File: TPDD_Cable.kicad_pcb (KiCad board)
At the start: 2 copper layers, 10.4 x 13.2 mm, 5 parts, among them J1 Wire Solder Pads, J2 TPDD, Q1 DTA114EKA, Q2 DTA114EKA, Q3 DTA114EKA

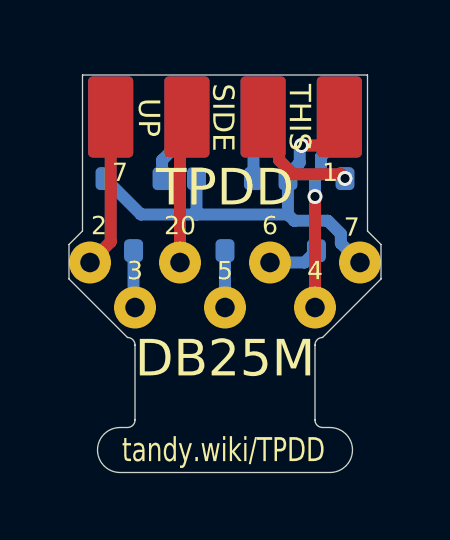
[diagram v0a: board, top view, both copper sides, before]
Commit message: kicad 6, ground zones
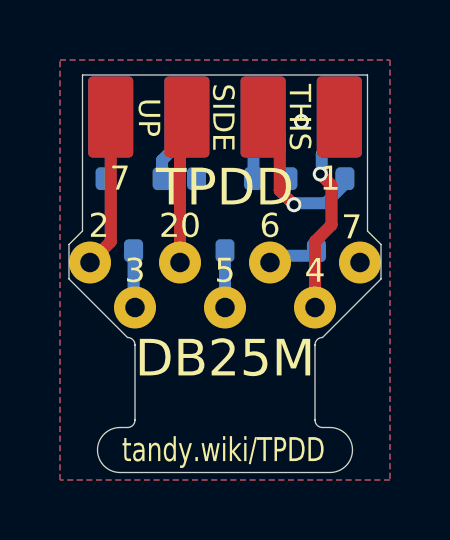
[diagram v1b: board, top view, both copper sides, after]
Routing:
- net /SG: track 15.6 -> 0.00 mm
- net /DSR_TTL: track 4.11 -> 5.51 mm
- added copper zone on B.Cu, net /SG
- added copper zone on F.Cu, net /SG
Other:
- net class Default removed
- board text added: "Q* ${00000000-0000-0000-0000-00005d2d4345:VALUE}"
- board text removed: "Q* DTA114EKA"
